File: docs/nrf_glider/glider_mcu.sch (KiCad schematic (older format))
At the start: 7 parts

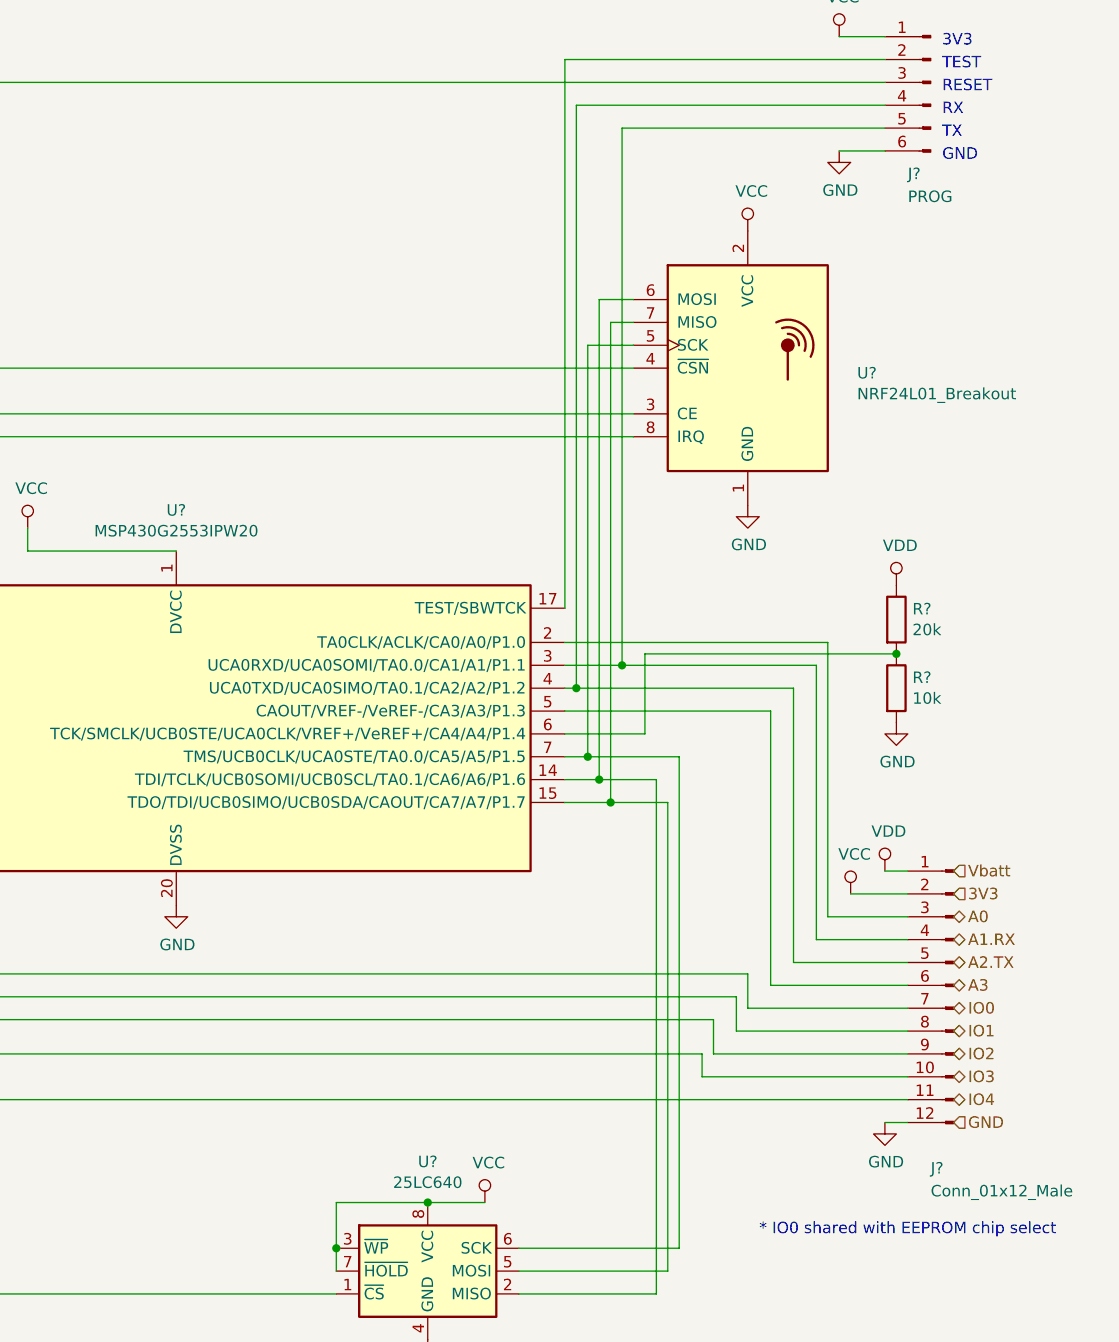
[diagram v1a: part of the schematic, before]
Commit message: remove and ignore bak files
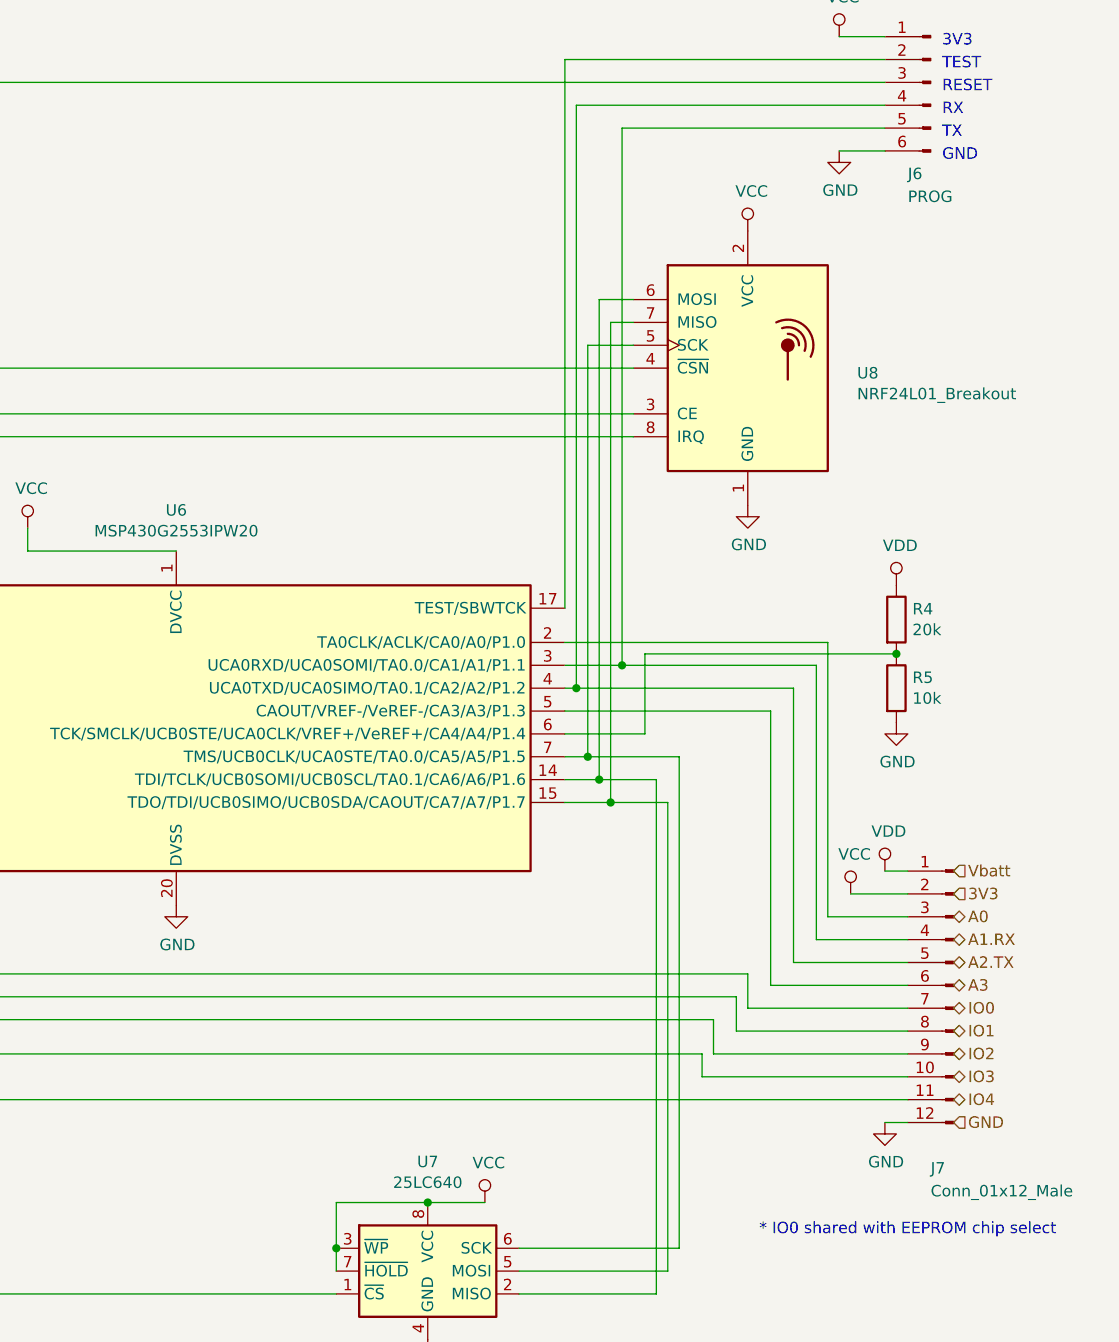
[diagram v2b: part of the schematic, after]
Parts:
- gave numbers to parts that had none: 7
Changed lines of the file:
@@
 $EndDescr
 $Comp
-L RF:NRF24L01_Breakout U?
+L RF:NRF24L01_Breakout U3
 U 1 1 5BCECC43
 P 5350 2300
-AR Path="/5BD3906D/5BCECC43" Ref="U?"  Part="1"
-AR Path="/5BD39338/5BCECC43" Ref="U?"  Part="1"
-F 0 "U?" H 5828 2278 50  0000 L CNN
+AR Path="/5BD3906D/5BCECC43" Ref="U3"  Part="1"
+AR Path="/5BD39338/5BCECC43" Ref="U8"  Part="1"
+F 0 "U8" H 5828 2278 50  0000 L CNN
 F 1 "NRF24L01_Breakout" H 5828 2187 50  0000 L CNN
 F 2 "RF_Module:nRF24L01_Breakout" H 5500 2900 50  0001 L CIN
@@
 $EndComp
 $Comp
-L MCU_Texas_MSP430:MSP430G2553IPW20 U?
+L MCU_Texas_MSP430:MSP430G2553IPW20 U1
 U 1 1 5BCECD91
 P 2850 3900
-AR Path="/5BD3906D/5BCECD91" Ref="U?"  Part="1"
-AR Path="/5BD39338/5BCECD91" Ref="U?"  Part="1"
-F 0 "U?" H 2850 4878 50  0000 C CNN
+AR Path="/5BD3906D/5BCECD91" Ref="U1"  Part="1"
+AR Path="/5BD39338/5BCECD91" Ref="U6"  Part="1"
+F 0 "U6" H 2850 4878 50  0000 C CNN
 F 1 "MSP430G2553IPW20" H 2850 4787 50  0000 C CNN
 F 2 "Package_DIP:DIP-20_W7.62mm" H 1400 3350 50  0001 C CIN
@@
 $EndComp
 $Comp
-L Memory_EEPROM:25LCxxx U?
+L Memory_EEPROM:25LCxxx U2
 U 1 1 5BCED472
 P 3950 6250
-AR Path="/5BD3906D/5BCED472" Ref="U?"  Part="1"
-AR Path="/5BD39338/5BCED472" Ref="U?"  Part="1"
-F 0 "U?" H 3950 6728 50  0000 C CNN
+AR Path="/5BD3906D/5BCED472" Ref="U2"  Part="1"
+AR Path="/5BD39338/5BCED472" Ref="U7"  Part="1"
+F 0 "U7" H 3950 6728 50  0000 C CNN
 F 1 "25LC640" H 3950 6637 50  0000 C CNN
 F 2 "Package_DIP:DIP-8_W7.62mm" H 3950 6250 50  0001 C CNN
@@
 	1100 3800 1150 3800
 $Comp
-L power:VCC #PWR?
+L power:VCC #PWR0101
 U 1 1 5BCEF2DA
 P 5350 1700
-AR Path="/5BD3906D/5BCEF2DA" Ref="#PWR?"  Part="1"
-AR Path="/5BD39338/5BCEF2DA" Ref="#PWR?"  Part="1"
-F 0 "#PWR?" H 5350 1550 50  0001 C CNN
+AR Path="/5BD3906D/5BCEF2DA" Ref="#PWR0101"  Part="1"
+AR Path="/5BD39338/5BCEF2DA" Ref="#PWR0141"  Part="1"
+F 0 "#PWR0141" H 5350 1550 50  0001 C CNN
 F 1 "VCC" H 5367 1873 50  0000 C CNN
 F 2 "" H 5350 1700 50  0001 C CNN
@@
 $EndComp
 $Comp
-L power:GND #PWR?
+L power:GND #PWR0102
 U 1 1 5BCEF357
 P 5350 2900
-AR Path="/5BD3906D/5BCEF357" Ref="#PWR?"  Part="1"
-AR Path="/5BD39338/5BCEF357" Ref="#PWR?"  Part="1"
-F 0 "#PWR?" H 5350 2650 50  0001 C CNN
+AR Path="/5BD3906D/5BCEF357" Ref="#PWR0102"  Part="1"
+AR Path="/5BD39338/5BCEF357" Ref="#PWR0142"  Part="1"
+F 0 "#PWR0142" H 5350 2650 50  0001 C CNN
 F 1 "GND" H 5355 2727 50  0000 C CNN
 F 2 "" H 5350 2900 50  0001 C CNN
@@
 $EndComp
 $Comp
-L power:GND #PWR?
+L power:GND #PWR0103
 U 1 1 5BCEF4A1
 P 3950 6550
-AR Path="/5BD3906D/5BCEF4A1" Ref="#PWR?"  Part="1"
-AR Path="/5BD39338/5BCEF4A1" Ref="#PWR?"  Part="1"
-F 0 "#PWR?" H 3950 6300 50  0001 C CNN
+AR Path="/5BD3906D/5BCEF4A1" Ref="#PWR0103"  Part="1"
+AR Path="/5BD39338/5BCEF4A1" Ref="#PWR0143"  Part="1"
+F 0 "#PWR0143" H 3950 6300 50  0001 C CNN
 F 1 "GND" H 3955 6377 50  0000 C CNN
 F 2 "" H 3950 6550 50  0001 C CNN
@@
 $EndComp
 $Comp
-L power:GND #PWR?
+L power:GND #PWR0104
 U 1 1 5BCEF4DF
 P 2850 4650
-AR Path="/5BD3906D/5BCEF4DF" Ref="#PWR?"  Part="1"
-AR Path="/5BD39338/5BCEF4DF" Ref="#PWR?"  Part="1"
-F 0 "#PWR?" H 2850 4400 50  0001 C CNN
+AR Path="/5BD3906D/5BCEF4DF" Ref="#PWR0104"  Part="1"
+AR Path="/5BD39338/5BCEF4DF" Ref="#PWR0144"  Part="1"
+F 0 "#PWR0144" H 2850 4400 50  0001 C CNN
 F 1 "GND" H 2855 4477 50  0000 C CNN
 F 2 "" H 2850 4650 50  0001 C CNN
@@
 $EndComp
 $Comp
-L power:VCC #PWR?
+L power:VCC #PWR0105
 U 1 1 5BCEF55C
 P 2200 3000
-AR Path="/5BD3906D/5BCEF55C" Ref="#PWR?"  Part="1"
-AR Path="/5BD39338/5BCEF55C" Ref="#PWR?"  Part="1"
-F 0 "#PWR?" H 2200 2850 50  0001 C CNN
+AR Path="/5BD3906D/5BCEF55C" Ref="#PWR0105"  Part="1"
+AR Path="/5BD39338/5BCEF55C" Ref="#PWR0145"  Part="1"
+F 0 "#PWR0145" H 2200 2850 50  0001 C CNN
 F 1 "VCC" H 2217 3173 50  0000 C CNN
 F 2 "" H 2200 3000 50  0001 C CNN
@@
 $EndComp
 $Comp
-L power:VCC #PWR?
+L power:VCC #PWR0106
 U 1 1 5BCEF5D9
 P 4200 5950
-AR Path="/5BD3906D/5BCEF5D9" Ref="#PWR?"  Part="1"
-AR Path="/5BD39338/5BCEF5D9" Ref="#PWR?"  Part="1"
-F 0 "#PWR?" H 4200 5800 50  0001 C CNN
+AR Path="/5BD3906D/5BCEF5D9" Ref="#PWR0106"  Part="1"
+AR Path="/5BD39338/5BCEF5D9" Ref="#PWR0146"  Part="1"
+F 0 "#PWR0146" H 4200 5800 50  0001 C CNN
 F 1 "VCC" H 4217 6123 50  0000 C CNN
 F 2 "" H 4200 5950 50  0001 C CNN
@@
 Connection ~ 4700 4100
 $Comp
-L Device:R R?
+L Device:R R1
 U 1 1 5BCF4A41
 P 6000 3400
-AR Path="/5BD3906D/5BCF4A41" Ref="R?"  Part="1"
-AR Path="/5BD39338/5BCF4A41" Ref="R?"  Part="1"
-F 0 "R?" H 6070 3446 50  0000 L CNN
+AR Path="/5BD3906D/5BCF4A41" Ref="R1"  Part="1"
+AR Path="/5BD39338/5BCF4A41" Ref="R4"  Part="1"
+F 0 "R4" H 6070 3446 50  0000 L CNN
 F 1 "20k" H 6070 3355 50  0000 L CNN
 F 2 "Resistor_THT:R_Axial_DIN0411_L9.9mm_D3.6mm_P12.70mm_Horizontal" V 5930 3400 50  0001 C CNN
@@
 $EndComp
 $Comp
-L Device:R R?
+L Device:R R2
 U 1 1 5BCF4AC6
 P 6000 3700
-AR Path="/5BD3906D/5BCF4AC6" Ref="R?"  Part="1"
-AR Path="/5BD39338/5BCF4AC6" Ref="R?"  Part="1"
-F 0 "R?" H 6070 3746 50  0000 L CNN
+AR Path="/5BD3906D/5BCF4AC6" Ref="R2"  Part="1"
+AR Path="/5BD39338/5BCF4AC6" Ref="R5"  Part="1"
+F 0 "R5" H 6070 3746 50  0000 L CNN
 F 1 "10k" H 6070 3655 50  0000 L CNN
 F 2 "Resistor_THT:R_Axial_DIN0411_L9.9mm_D3.6mm_P12.70mm_Horizontal" V 5930 3700 50  0001 C CNN
@@
 $EndComp
 $Comp
-L power:GND #PWR?
+L power:GND #PWR0107
 U 1 1 5BCF4B6F
 P 6000 3850
-AR Path="/5BD3906D/5BCF4B6F" Ref="#PWR?"  Part="1"
-AR Path="/5BD39338/5BCF4B6F" Ref="#PWR?"  Part="1"
-F 0 "#PWR?" H 6000 3600 50  0001 C CNN
+AR Path="/5BD3906D/5BCF4B6F" Ref="#PWR0107"  Part="1"
+AR Path="/5BD39338/5BCF4B6F" Ref="#PWR0147"  Part="1"
+F 0 "#PWR0147" H 6000 3600 50  0001 C CNN
 F 1 "GND" H 6005 3677 50  0000 C CNN
 F 2 "" H 6000 3850 50  0001 C CNN
@@
 Connection ~ 6000 3550
 $Comp
-L power:VDD #PWR?
+L power:VDD #PWR0108
 U 1 1 5BCF63D1
 P 6000 3250
-AR Path="/5BD3906D/5BCF63D1" Ref="#PWR?"  Part="1"
-AR Path="/5BD39338/5BCF63D1" Ref="#PWR?"  Part="1"
-F 0 "#PWR?" H 6000 3100 50  0001 C CNN
+AR Path="/5BD3906D/5BCF63D1" Ref="#PWR0108"  Part="1"
+AR Path="/5BD39338/5BCF63D1" Ref="#PWR0148"  Part="1"
+F 0 "#PWR0148" H 6000 3100 50  0001 C CNN
 F 1 "VDD" H 6017 3423 50  0000 C CNN
 F 2 "" H 6000 3250 50  0001 C CNN
@@
 $EndComp
 $Comp
-L Connector:Conn_01x12_Male J?
+L Connector:Conn_01x12_Male J2
 U 1 1 5BCFA9FB
 P 6250 5000
-AR Path="/5BD3906D/5BCFA9FB" Ref="J?"  Part="1"
-AR Path="/5BD39338/5BCFA9FB" Ref="J?"  Part="1"
-F 0 "J?" H 6350 4200 50  0000 R CNN
+AR Path="/5BD3906D/5BCFA9FB" Ref="J2"  Part="1"
+AR Path="/5BD39338/5BCFA9FB" Ref="J7"  Part="1"
+F 0 "J7" H 6350 4200 50  0000 R CNN
 F 1 "Conn_01x12_Male" H 6350 4100 50  0000 R CNN
 F 2 "Connector_PinHeader_2.54mm:PinHeader_1x12_P2.54mm_Vertical" H 6250 5000 50  0001 C CNN
@@
 $EndComp
 $Comp
-L power:VDD #PWR?
+L power:VDD #PWR0109
 U 1 1 5BCFAD35
 P 5950 4500
-AR Path="/5BD3906D/5BCFAD35" Ref="#PWR?"  Part="1"
-AR Path="/5BD39338/5BCFAD35" Ref="#PWR?"  Part="1"
-F 0 "#PWR?" H 5950 4350 50  0001 C CNN
+AR Path="/5BD3906D/5BCFAD35" Ref="#PWR0109"  Part="1"
+AR Path="/5BD39338/5BCFAD35" Ref="#PWR0149"  Part="1"
+F 0 "#PWR0149" H 5950 4350 50  0001 C CNN
 F 1 "VDD" H 5967 4673 50  0000 C CNN
 F 2 "" H 5950 4500 50  0001 C CNN
@@
 	5950 4500 6050 4500
 $Comp
-L power:VCC #PWR?
+L power:VCC #PWR0110
 U 1 1 5BCFB594
 P 5800 4600
-AR Path="/5BD3906D/5BCFB594" Ref="#PWR?"  Part="1"
-AR Path="/5BD39338/5BCFB594" Ref="#PWR?"  Part="1"
-F 0 "#PWR?" H 5800 4450 50  0001 C CNN
+AR Path="/5BD3906D/5BCFB594" Ref="#PWR0110"  Part="1"
+AR Path="/5BD39338/5BCFB594" Ref="#PWR0150"  Part="1"
+F 0 "#PWR0150" H 5800 4450 50  0001 C CNN
 F 1 "VCC" H 5817 4773 50  0000 C CNN
 F 2 "" H 5800 4600 50  0001 C CNN
@@
 	5800 4600 6050 4600
 $Comp
-L power:GND #PWR?
+L power:GND #PWR0111
 U 1 1 5BCFBE51
 P 5950 5600
-AR Path="/5BD3906D/5BCFBE51" Ref="#PWR?"  Part="1"
-AR Path="/5BD39338/5BCFBE51" Ref="#PWR?"  Part="1"
-F 0 "#PWR?" H 5950 5350 50  0001 C CNN
+AR Path="/5BD3906D/5BCFBE51" Ref="#PWR0111"  Part="1"
+AR Path="/5BD39338/5BCFBE51" Ref="#PWR0151"  Part="1"
+F 0 "#PWR0151" H 5950 5350 50  0001 C CNN
 F 1 "GND" H 5955 5427 50  0000 C CNN
 F 2 "" H 5950 5600 50  0001 C CNN
@@
 MCU Module
 $Comp
-L Connector:Conn_01x06_Male J?
+L Connector:Conn_01x06_Male J1
 U 1 1 5BD41D4E
 P 6150 1050
-AR Path="/5BD3906D/5BD41D4E" Ref="J?"  Part="1"
-AR Path="/5BD39338/5BD41D4E" Ref="J?"  Part="1"
-F 0 "J?" H 6250 650 50  0000 R CNN
+AR Path="/5BD3906D/5BD41D4E" Ref="J1"  Part="1"
+AR Path="/5BD39338/5BD41D4E" Ref="J6"  Part="1"
+F 0 "J6" H 6250 650 50  0000 R CNN
 F 1 "PROG" H 6250 550 50  0000 R CNN
 F 2 "Connector_PinHeader_2.54mm:PinHeader_1x06_P2.54mm_Vertical" H 6150 1050 50  0001 C CNN
@@
 $EndComp
 $Comp
-L power:VCC #PWR?
+L power:VCC #PWR0112
 U 1 1 5BD421B2
 P 5750 850
-AR Path="/5BD3906D/5BD421B2" Ref="#PWR?"  Part="1"
-AR Path="/5BD39338/5BD421B2" Ref="#PWR?"  Part="1"
-F 0 "#PWR?" H 5750 700 50  0001 C CNN
+AR Path="/5BD3906D/5BD421B2" Ref="#PWR0112"  Part="1"
+AR Path="/5BD39338/5BD421B2" Ref="#PWR0152"  Part="1"
+F 0 "#PWR0152" H 5750 700 50  0001 C CNN
 F 1 "VCC" H 5767 1023 50  0000 C CNN
 F 2 "" H 5750 850 50  0001 C CNN
@@
 	5750 850  5950 850
 $Comp
-L power:GND #PWR?
+L power:GND #PWR0113
 U 1 1 5BD44828
 P 5750 1350
-AR Path="/5BD3906D/5BD44828" Ref="#PWR?"  Part="1"
-AR Path="/5BD39338/5BD44828" Ref="#PWR?"  Part="1"
-F 0 "#PWR?" H 5750 1100 50  0001 C CNN
+AR Path="/5BD3906D/5BD44828" Ref="#PWR0113"  Part="1"
+AR Path="/5BD39338/5BD44828" Ref="#PWR0153"  Part="1"
+F 0 "#PWR0153" H 5750 1100 50  0001 C CNN
 F 1 "GND" H 5755 1177 50  0000 C CNN
 F 2 "" H 5750 1350 50  0001 C CNN

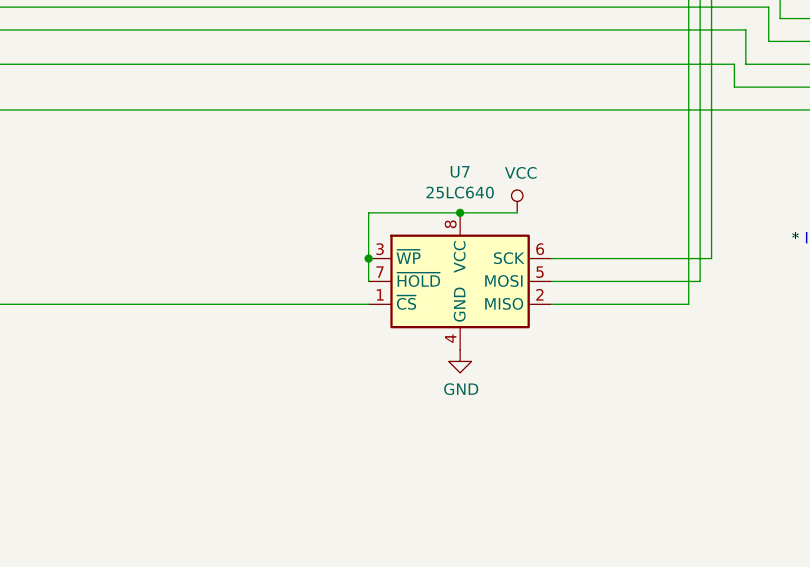
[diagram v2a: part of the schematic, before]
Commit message: fixed /WP pin on EEPROM
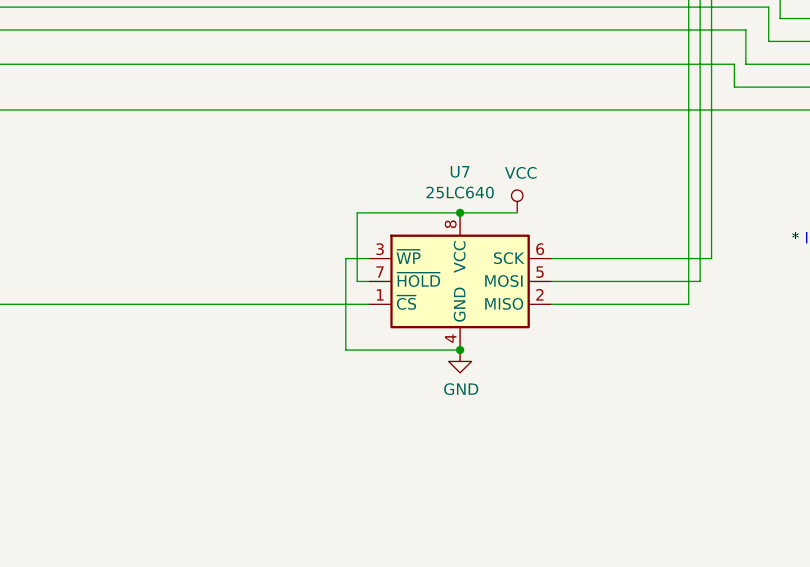
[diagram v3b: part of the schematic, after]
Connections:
- net GND: now also U2.3 (~WP)
- net VCC: no longer U2.3 (~WP)
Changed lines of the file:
@@
 EESchema Schematic File Version 4
-LIBS:nrf_glider-cache
+LIBS:glider_mcu-cache
 EELAYER 26 0
 EELAYER END
 $Descr A4 11693 8268
 encoding utf-8
-Sheet 1 5
+Sheet 1 1
 Title ""
 Date ""
@@
 AR Path="/5BD3906D/5BCED472" Ref="U2"  Part="1"
 AR Path="/5BD39338/5BCED472" Ref="U7"  Part="1"
+AR Path="/5BCED472" Ref="U7"  Part="1"
 F 0 "U7" H 3950 6728 50  0000 C CNN
 F 1 "25LC640" H 3950 6637 50  0000 C CNN
@@
 Text Notes 10300 7350 0    50   ~ 0
 created by Toby Kurien
-Wire Wire Line
-	3550 6250 3550 6150
-Wire Wire Line
-	3550 6150 3550 5950
-Connection ~ 3550 6150
-Connection ~ 3950 5950
-Wire Wire Line
-	3550 5950 3950 5950
-Wire Wire Line
-	3950 5950 4200 5950
 Text HLabel 6250 4500 2    50   Input ~ 0
 Vbatt
@@
 Text HLabel 6250 5600 2    50   Input ~ 0
 GND
+Wire Wire Line
+	3950 5950 4200 5950
+Wire Wire Line
+	3950 6550 3450 6550
+Wire Wire Line
+	3450 6550 3450 6150
+Wire Wire Line
+	3450 6150 3550 6150
+Connection ~ 3950 6550
+Wire Wire Line
+	3550 6250 3500 6250
+Wire Wire Line
+	3500 6250 3500 5950
+Wire Wire Line
+	3500 5950 3950 5950
+Connection ~ 3950 5950
 $EndSCHEMATC
